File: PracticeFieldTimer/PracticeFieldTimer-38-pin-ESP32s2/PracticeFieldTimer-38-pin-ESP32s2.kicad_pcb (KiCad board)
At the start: 2 copper layers, 140.1 x 160 mm, 28 parts, among them J1 External Controls, J2 4 x 20 I2C LCD, J3 Panel, J4 DS3231 Module, J5 /CAN Enable, J6 RJ45, J7 RJ45, J8 CAN Terminate, U1 ESP32-DevKitC, U2 SN65HVD230DR

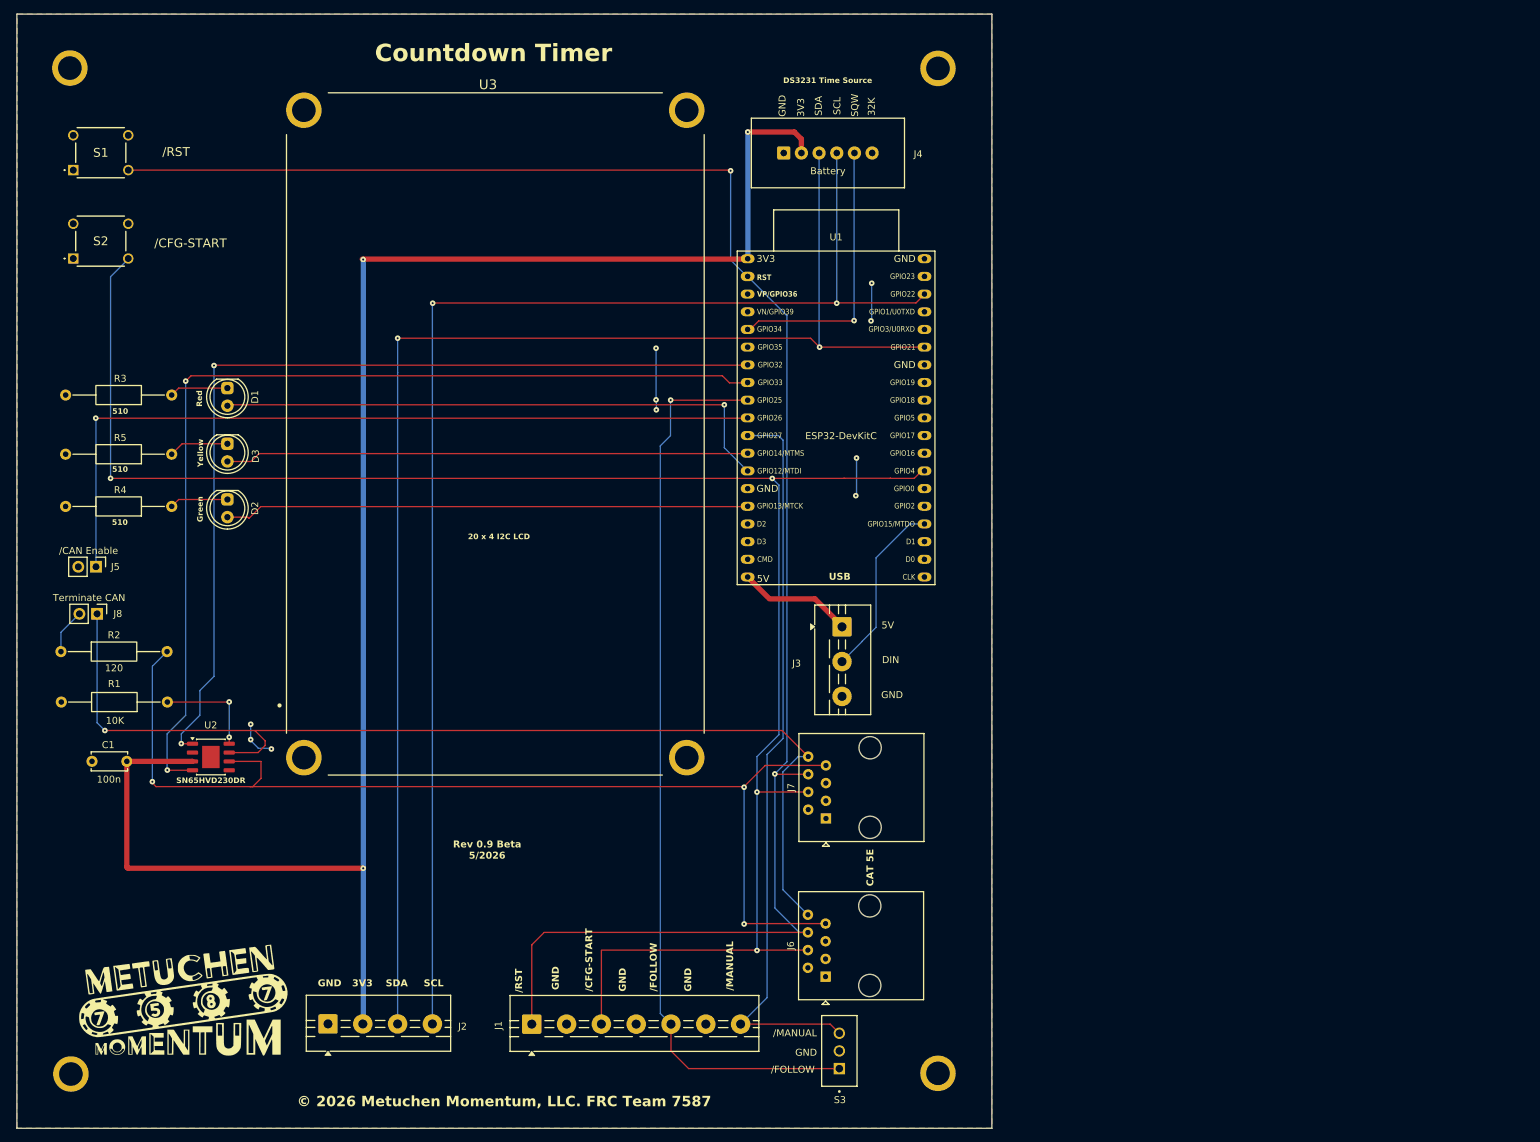
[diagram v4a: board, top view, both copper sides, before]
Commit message: Round the PCB corners, set the fill copper back from the edge, Align text, change to clear LEDs on 3-D view to avoid confusion.
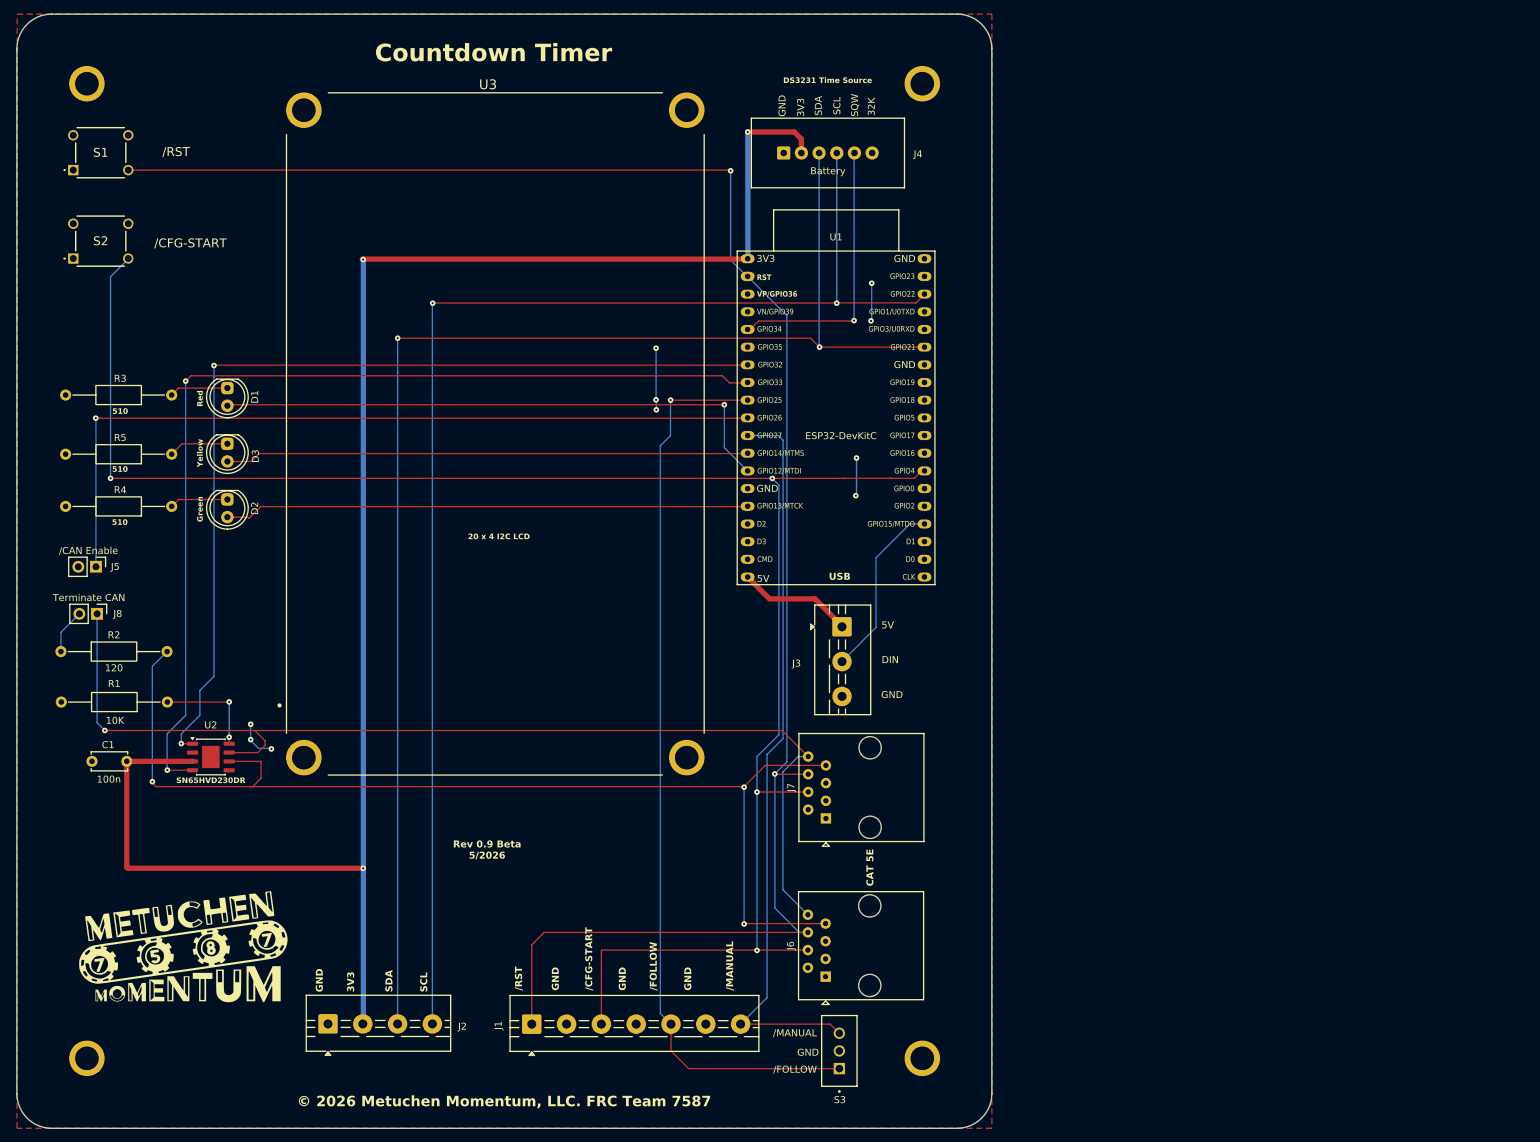
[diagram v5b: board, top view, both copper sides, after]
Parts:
- moved G*** 7.67 mm to (38.8, 154.0)
- moved ? 3.33 mm to (25.0, 30.0)
- moved ? 3.22 mm to (25.0, 170.0)
- moved ? 3.15 mm to (145.0, 30.0)
- moved ? 3.11 mm to (145.0, 170.0)
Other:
- outline, holes or cut-outs redrawn
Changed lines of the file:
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@@
 		)
 		(embedded_fonts no)
-		(model "${KICAD9_3DMODEL_DIR}/LED_THT.3dshapes/LED_D5.0mm.step"
+		(model "${KICAD9_3DMODEL_DIR}/LED_THT.3dshapes/LED_D5.0mm_Clear.step"
 			(offset
 				(xyz 0 0 0)
@@
 		)
 		(embedded_fonts no)
-		(model "${KICAD9_3DMODEL_DIR}/LED_THT.3dshapes/LED_D5.0mm.step"
+		(model "${KICAD9_3DMODEL_DIR}/LED_THT.3dshapes/LED_D5.0mm_Clear.step"
 			(offset
 				(xyz 0 0 0)
@@
 		)
 		(embedded_fonts no)
-		(model "${KICAD9_3DMODEL_DIR}/LED_THT.3dshapes/LED_D5.0mm.step"
+		(model "${KICAD9_3DMODEL_DIR}/LED_THT.3dshapes/LED_D5.0mm_Clear.step"
 			(offset
 				(xyz 0 0 0)
@@
 	(footprint ""
 		(layer "F.Cu")
-		(at 22.55 27.75)
+		(at 25 30)
 		(property "Reference" ""
 			(at 0 0 0)
@@
 	(footprint ""
 		(layer "F.Cu")
-		(at 22.7 172.25)
+		(at 25 170)
 		(property "Reference" ""
 			(at 0 0 0)
@@
 	(footprint ""
 		(layer "F.Cu")
-		(at 147.25 172.15)
+		(at 145 170)
 		(property "Reference" ""
 			(at 0 0 0)
@@
 	(footprint ""
 		(layer "F.Cu")
-		(at 147.25 27.8)
+		(at 145 30)
 		(property "Reference" ""
 			(at 0 0 0)
@@
 	(footprint "Misc:MetuchenMomentumLogo"
 		(layer "F.Cu")
-		(at 38.833523 161.671406)
+		(at 38.833523 154)
 		(property "Reference" "G***"
 			(at 0 0 0)
@@
 		)
 	)
-	(gr_rect
-		(start 14.939863 19.998876)
-		(end 154.989863 180.048676)
+	(gr_line
+		(start 14.939863 175.048676)
+		(end 14.939863 24.998876)
+		(stroke
+			(width 0.05)
+			(type default)
+		)
+		(layer "Edge.Cuts")
+	)
+	(gr_line
+		(start 19.939863 19.998876)
+		(end 149.989863 19.998876)
+		(stroke
+			(width 0.05)
+			(type default)
+		)
+		(layer "Edge.Cuts")
+	)
+	(gr_arc
+		(start 149.989863 19.998876)
+		(mid 153.525429 21.463328)
+		(end 154.989863 24.998876)
+		(stroke
+			(width 0.05)
+			(type default)
+		)
+		(layer "Edge.Cuts")
+	)
+	(gr_line
+		(start 154.989863 24.998876)
+		(end 154.989863 175.048676)
+		(stroke
+			(width 0.05)
+			(type default)
+		)
+		(layer "Edge.Cuts")
+	)
+	(gr_line
+		(start 149.989863 180.048676)
+		(end 19.939863 180.048676)
+		(stroke
+			(width 0.05)
+			(type default)
+		)
+		(layer "Edge.Cuts")
+	)
+	(gr_arc
+		(start 14.939863 24.998876)
+		(mid 16.404331 21.463346)
+		(end 19.939863 19.998876)
+		(stroke
+			(width 0.05)
+			(type default)
+		)
+		(layer "Edge.Cuts")
+	)
+	(gr_arc
+		(start 154.989863 175.048676)
+		(mid 153.525397 178.58421)
+		(end 149.989863 180.048676)
+		(stroke
+			(width 0.05)
+			(type default)
+		)
+		(layer "Edge.Cuts")
+	)
+	(gr_arc
+		(start 19.939863 180.048676)
+		(mid 16.404329 178.58421)
+		(end 14.939863 175.048676)
 		(stroke
 			(width 0.05)
 			(type default)
 		)
-		(fill no)
 		(layer "Edge.Cuts")
 	)
 	(gr_text "GND"
-		(at 102.526463 160.410076 90)
+		(at 102.526463 160.283076 90)
 		(layer "F.SilkS")
 		(effects
@@
 	)
 	(gr_text "3V3"
-		(at 63.080263 159.775076 0)
+		(at 63.5 160.5 90)
 		(layer "F.SilkS")
 		(effects
@@
 	)
 	(gr_text "5V"
-		(at 140.042263 107.781276 0)
+		(at 140.032816 107.781276 0)
 		(layer "F.SilkS")
 		(effects
@@
 	)
 	(gr_text "Yellow"
-		(at 41.312463 83.041676 90)
+		(at 41.261663 83.041676 90)
 		(layer "F.SilkS")
 		(effects
@@
 	)
 	(gr_text "GND"
-		(at 111.340263 160.410076 90)
+		(at 111.340263 160.283076 90)
 		(layer "F.SilkS")
 		(effects
@@
 	)
 	(gr_text "/FOLLOW"
-		(at 106.387263 160.410076 90)
+		(at 106.387263 160.283076 90)
 		(layer "F.SilkS")
 		(effects
@@
 	)
 	(gr_text "/FOLLOW"
-		(at 126.4 171.6 0)
+		(at 126.728609 171.6 0)
 		(layer "F.SilkS")
 		(effects
@@
 	)
 	(gr_text "GND"
-		(at 58.152663 159.775076 0)
+		(at 59 160.5 90)
 		(layer "F.SilkS")
 		(effects
@@
 	)
 	(gr_text "SCL"
-		(at 73.367263 159.775076 0)
+		(at 74 160.5 90)
 		(layer "F.SilkS")
 		(effects
@@
 	)
 	(gr_text "SDA"
-		(at 67.906263 159.775076 0)
+		(at 69 160.5 90)
 		(layer "F.SilkS")
 		(effects
@@
 	)
 	(gr_text "/RST"
-		(at 87.032463 160.587876 90)
+		(at 87.032463 160.283076 90)
 		(layer "F.SilkS")
 		(effects
@@
 	)
 	(gr_text "/CFG-START"
-		(at 97.119063 160.428676 90)
+		(at 97.119063 160.283076 90)
 		(layer "F.SilkS")
 		(effects
@@
 	)
 	(gr_text "GND"
-		(at 92.315663 160.181476 90)
+		(at 92.315663 160.283076 90)
 		(layer "F.SilkS")
 		(effects
@@
 	)
 	(gr_text "DIN"
-		(at 140.448663 112.759676 0)
+		(at 140.389958 112.759676 0)
 		(layer "F.SilkS")
 		(effects
@@
 	)
 	(gr_text "Red"
-		(at 41.160063 75.218476 90)
+		(at 41.261663 75.218476 90)
 		(layer "F.SilkS")
 		(effects
@@
 	)
 	(gr_text "GND"
-		(at 128.305 169.1616 0)
+		(at 128.585752 169.1616 0)
 		(layer "F.SilkS")
 		(effects
